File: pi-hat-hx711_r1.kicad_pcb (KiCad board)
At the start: 4 copper layers, 65 x 56 mm, 53 parts, among them J1 GPIO, J2 Conn_01x06, J3 Conn_01x06, J4 Conn_01x06, J5 Conn_01x06, Q1 S8550, U1 M24c64, U2 HX711, U4 TPS61040DBV, U5 TPS7A2050PDBV

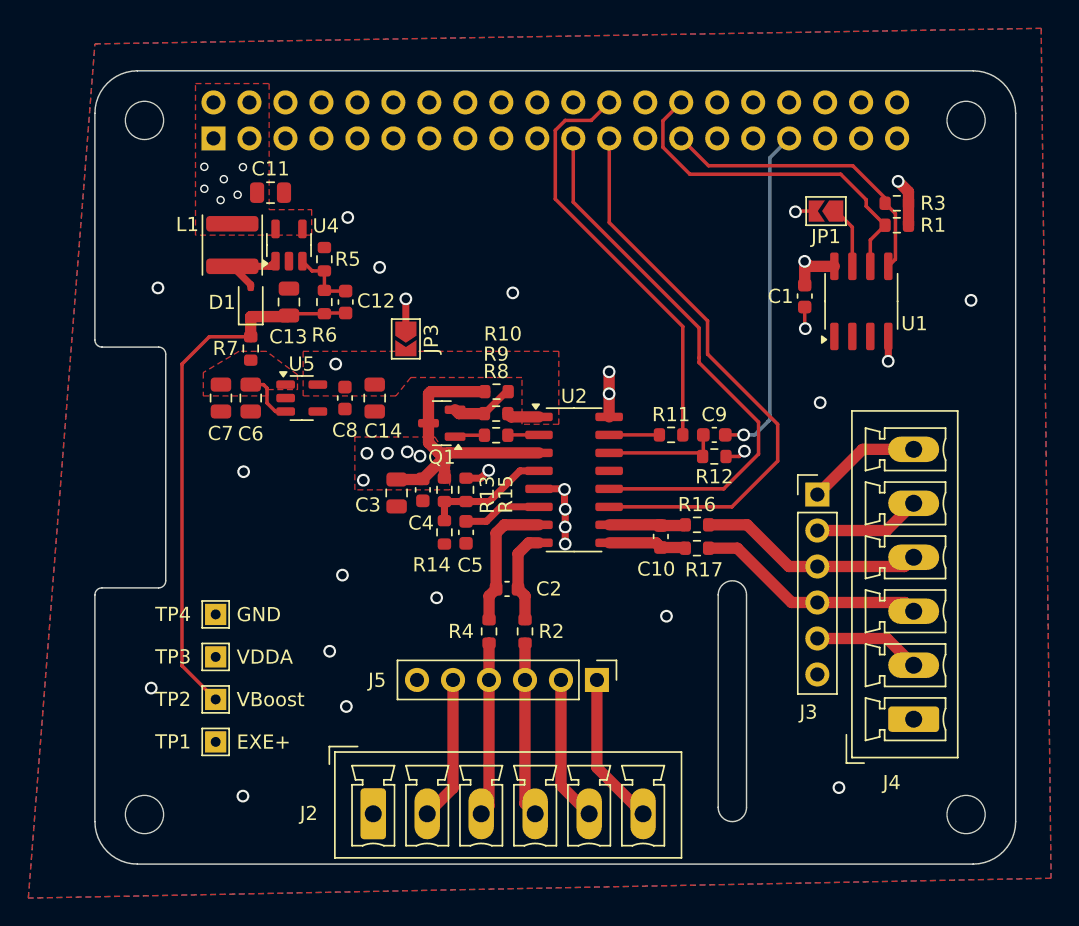
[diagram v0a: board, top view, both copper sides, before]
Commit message: wheeww!
Added 3.3v supply from 5V by default.
Added header to access IOs without rpi
Added TP to supply/monitor raw 5V (use without pi)
Adjusted TPs to be on 2.54mm spacing to get headers if desired
Added TVS on EXE+ lines.
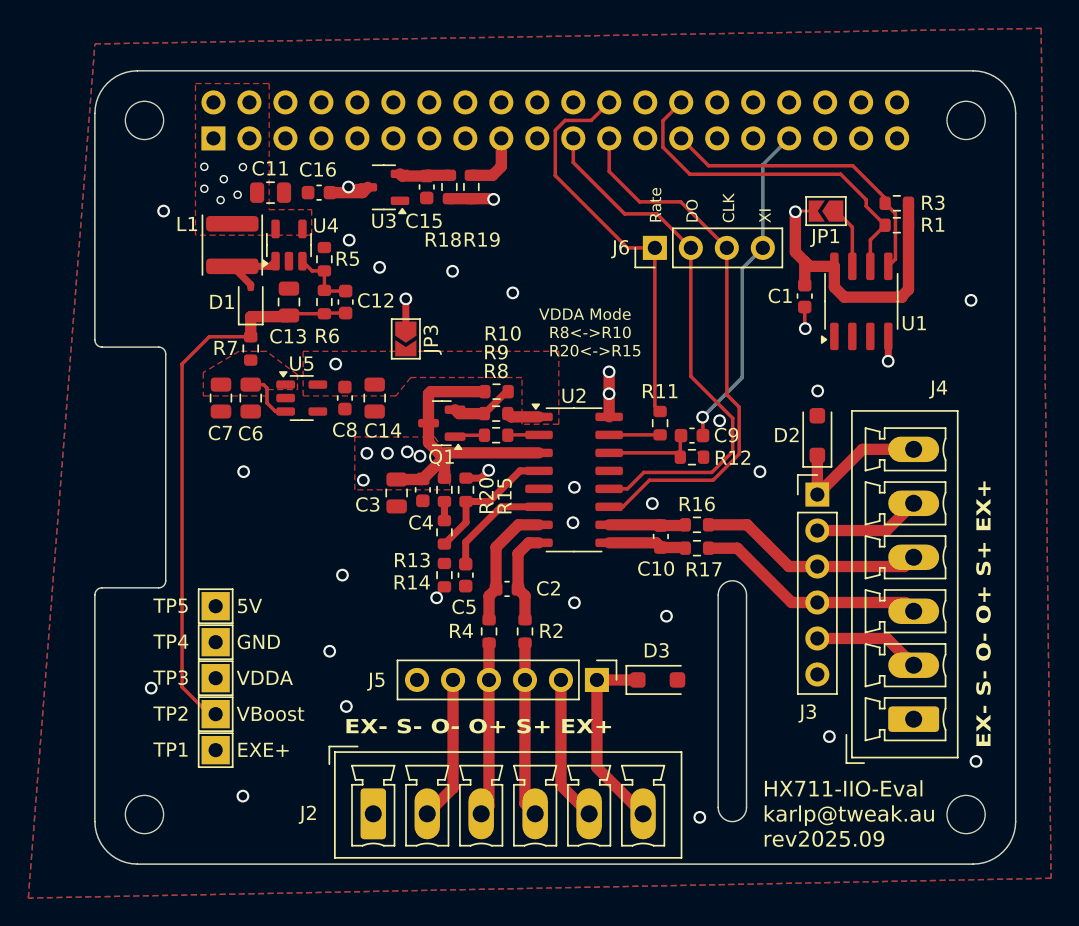
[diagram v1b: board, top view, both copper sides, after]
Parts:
- added C15: 1uF, Capacitor_SMD:C_0603_1608Metric, F.Cu at (123.4, 52.2)
- added C16: 1uF, Capacitor_SMD:C_0603_1608Metric, F.Cu at (115.8, 52.6)
- added D2: SMF5.0A, Diode_SMD:D_SOD-123F, F.Cu at (151.0, 69.8)
- added D3: SMF5.0A, Diode_SMD:D_SOD-123F, F.Cu at (139.7, 87.0)
- added J6: Conn_01x04, Connector_PinHeader_2.54mm:PinHeader_1x04_P2.54mm_Vertical, F.Cu at (139.5, 56.5)
- added R18: 0R, Resistor_SMD:R_0603_1608Metric, F.Cu at (125.0, 52.2)
- added R19: 0R, Resistor_SMD:R_0603_1608Metric, F.Cu at (126.6, 52.2)
- added R20: 0R, Resistor_SMD:R_0603_1608Metric, F.Cu at (124.7, 73.6)
- added TP5: TestPoint, TestPoint:TestPoint_THTPad_2.0x2.0mm_Drill1.0mm, F.Cu at (108.5, 81.8)
- added U3: XC6206P332MR, Package_TO_SOT_SMD:SOT-23-3, F.Cu at (120.4, 52.2)
- TP1, TP2, TP3, TP4: footprint TestPoint:TestPoint_THTPad_1.5x1.5mm_Drill0.7mm -> TestPoint:TestPoint_THTPad_2.0x2.0mm_Drill1.0mm
- moved C5 3.02 mm to (126.2, 79.6)
- moved R14 3.02 mm to (124.7, 79.6)
- moved R13 3.00 mm to (124.7, 76.6)
- moved TP4 1.96 mm to (108.5, 84.3)
- moved R12 1.58 mm to (142.2, 71.3)
- moved C9 1.58 mm to (142.2, 69.8)
- moved TP3 1.50 mm to (108.5, 86.9)
- moved R11 1.13 mm to (139.9, 68.9), turned to 90 degrees
- moved TP2 1.04 mm to (108.5, 89.4)
- moved TP1 0.58 mm to (108.5, 92.0)
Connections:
- J1 pad 1: +3V3 -> /3v3pi
- J1 pad 17: +3V3 -> /3v3pi
- R13 pad 1: /EXE1+ -> Net-(R13-Pad1)
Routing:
- net +3V3: track 12.0 -> 66.3 mm, vias 5 -> 4
- net +5V: track 20.2 -> 53.4 mm, vias 7 -> 8
- net /EXE1+: track 110.0 -> 116.8 mm
- net GND: track 12.3 -> 5.56 mm, vias 23 -> 27
- net /3v3pi: track 0.00 -> 4.36 mm
- net Net-(U3-VO): track 0.00 -> 3.57 mm
- net VDDA: track 27.2 -> 29.8 mm
- net /GPIO11/SPI0.SCLK: track 40.9 -> 38.5 mm
- net Net-(U2-VBG): track 5.57 -> 7.76 mm
- net Net-(U2-XI): track 8.25 -> 6.70 mm
- net /GPIO9/SPI0.MISO: track 39.3 -> 37.9 mm
- net Net-(R13-Pad1): track 0.00 -> 1.35 mm
- net /power/VBOOST: track 38.5 -> 39.8 mm
- net /GPIO8/SPI0.CE0: track 29.9 -> 28.7 mm
- net Net-(U2-VFB): track 8.92 -> 9.68 mm
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- removed copper zone on In2.Cu, net +3V3
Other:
- board text added: "5V"
- board text added: "EX- S- O- O+ S+ EX+"
- board text added: "HX711-IIO-Eval karlp@tweak.au rev2025.09"
- board text added: "Rate DO CLK XI"
- board text added: "VDDA Mode R8<->R10 R20<->R15"

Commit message: erc/drc cleanups
fix lots of off grid stuff that got dragged off in earlier
re-arrangements
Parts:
- moved L1 0.35 mm to (109.3, 56.3)
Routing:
- net GND: track 5.56 -> 9.76 mm
- net Net-(U2-VFB): track 9.68 -> 11.0 mm
- net +3V3: vias 4 -> 3
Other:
- board text added: "ChA"
- board text added: "ChB"

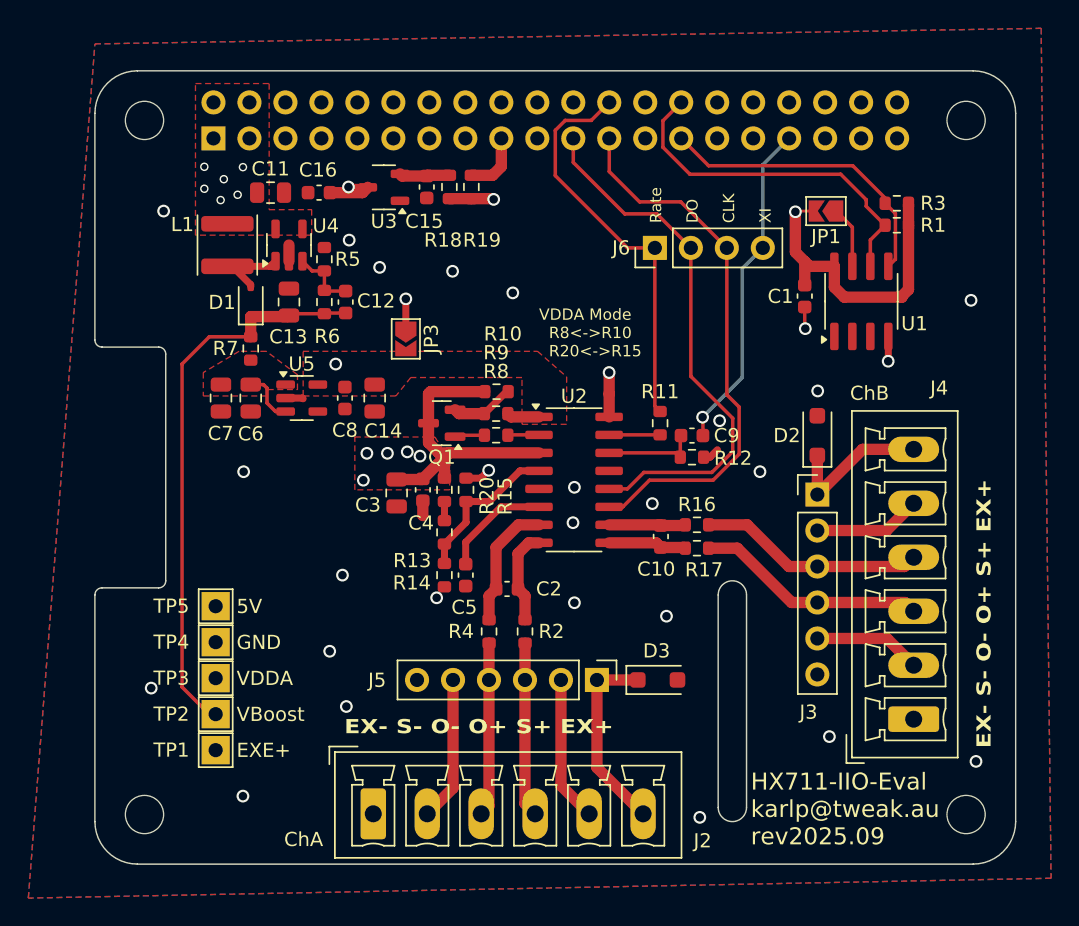
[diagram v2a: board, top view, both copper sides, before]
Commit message: adds a 2 pin power in connector
I don't have any suitable power supplies for RPi, so just put on a
connector to use external if desired.  Totally raw unprotected, just
feeds straight to the rpi.
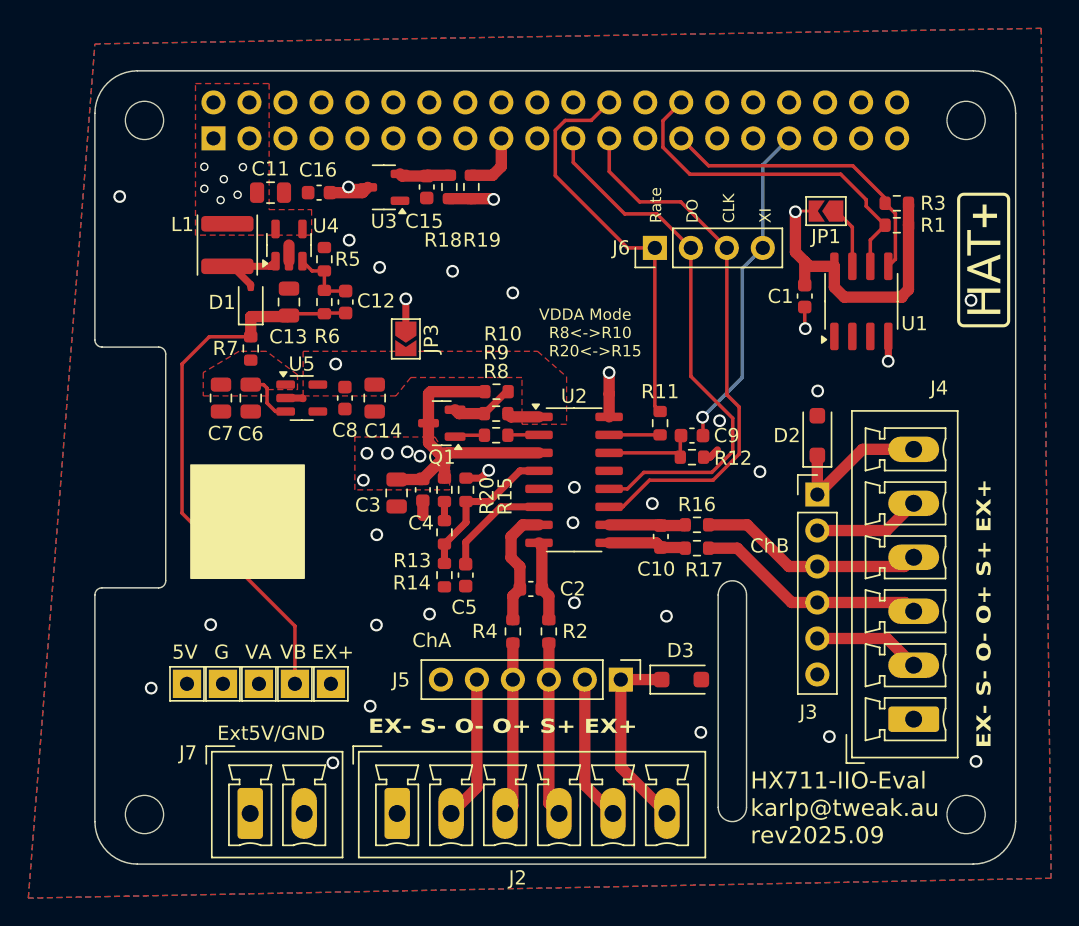
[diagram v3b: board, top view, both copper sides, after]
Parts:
- added J7: Conn_01x02, Connector_Phoenix_MC:PhoenixContact_MCV_1,5_2-G-3.81_1x02_P3.81mm_Vertical, F.Cu at (111.0, 96.4)
- added X1: ~, jlc-extras:JLC_2D_BARCODE_8x8mm, F.Cu at (110.8, 75.8)
- moved TP1 9.39 mm to (116.7, 87.3), turned to 90 degrees
- moved TP2 5.99 mm to (114.1, 87.3), turned to 90 degrees
- moved TP5 5.84 mm to (106.5, 87.3), turned to 90 degrees
- moved TP3 3.08 mm to (111.6, 87.3), turned to 90 degrees
- moved TP4 2.98 mm to (109.0, 87.3), turned to 90 degrees
- moved D3 1.69 mm to (141.4, 87.0)
- moved J5 1.69 mm to (137.1, 87.0)
- moved J2 1.69 mm to (121.3, 96.4)
- moved C2 1.68 mm to (130.8, 80.6)
- moved R4 1.68 mm to (129.5, 83.6)
- moved R2 1.68 mm to (132.0, 83.6)
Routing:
- net +5V: track 53.4 -> 70.9 mm
- net /EXE1+: track 116.8 -> 108.2 mm
- net VDDA: track 29.8 -> 27.1 mm
- net /Analog/IN1+: track 6.67 -> 5.72 mm
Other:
- board text added: "EX+"
- board text added: "Ext5V/GND"
- board text added: "G"
- board text added: "VA"
- board text added: "VB"
- board text removed: "EXE+"
- board text removed: "GND"
- board text removed: "VBoost"
- board text removed: "VDDA"
